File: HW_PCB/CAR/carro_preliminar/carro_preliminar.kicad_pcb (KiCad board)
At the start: 2 copper layers, 53.7 x 34.7 mm, 38 parts, among them IC1 TB6612FNG, J1 V_Battery, J2 STLINK, J3 Motores, J5 UART, J6 Servo_Motor, J7 Conn_02x04_Odd_Even, SW1 SW_DPST_x2, U1 STM32F103C8Tx, U2 AMS1117-3.3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

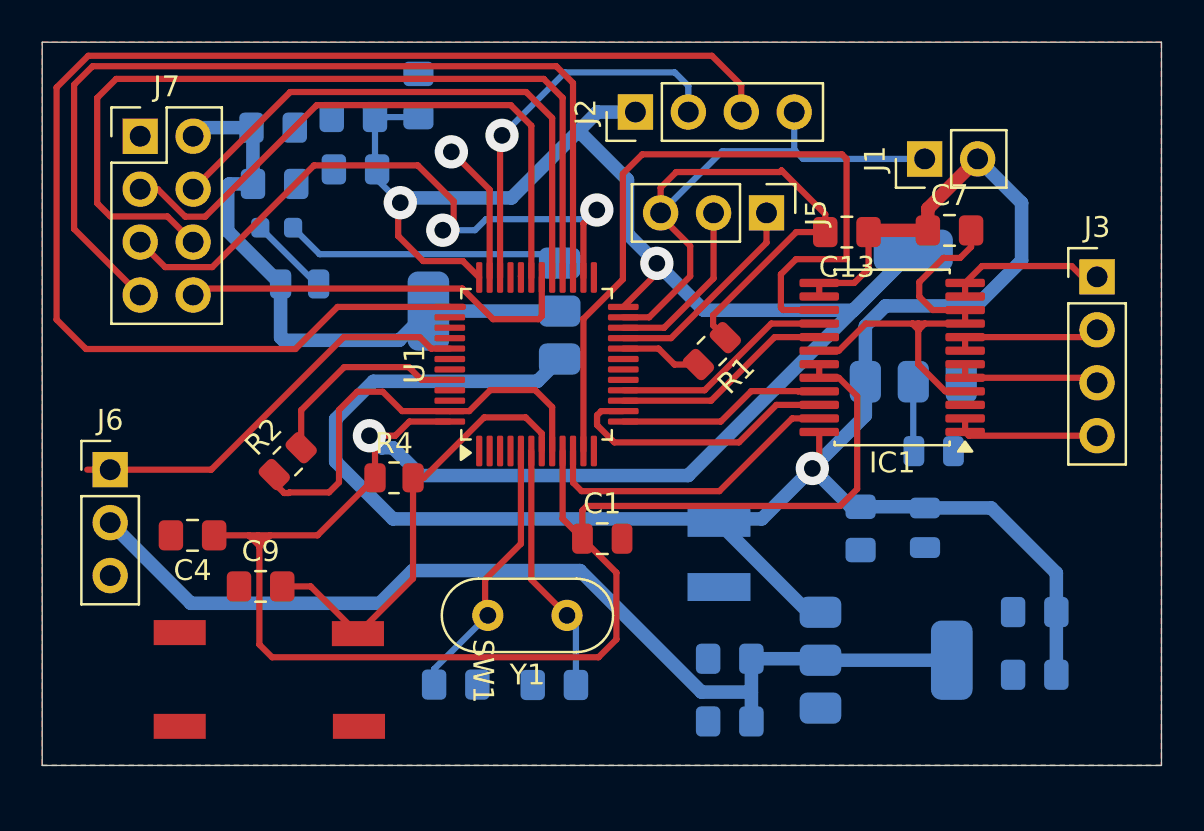
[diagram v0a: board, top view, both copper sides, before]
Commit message: Añadido divisor de tension para bateria, y conectir para luces indicadoras de bateria
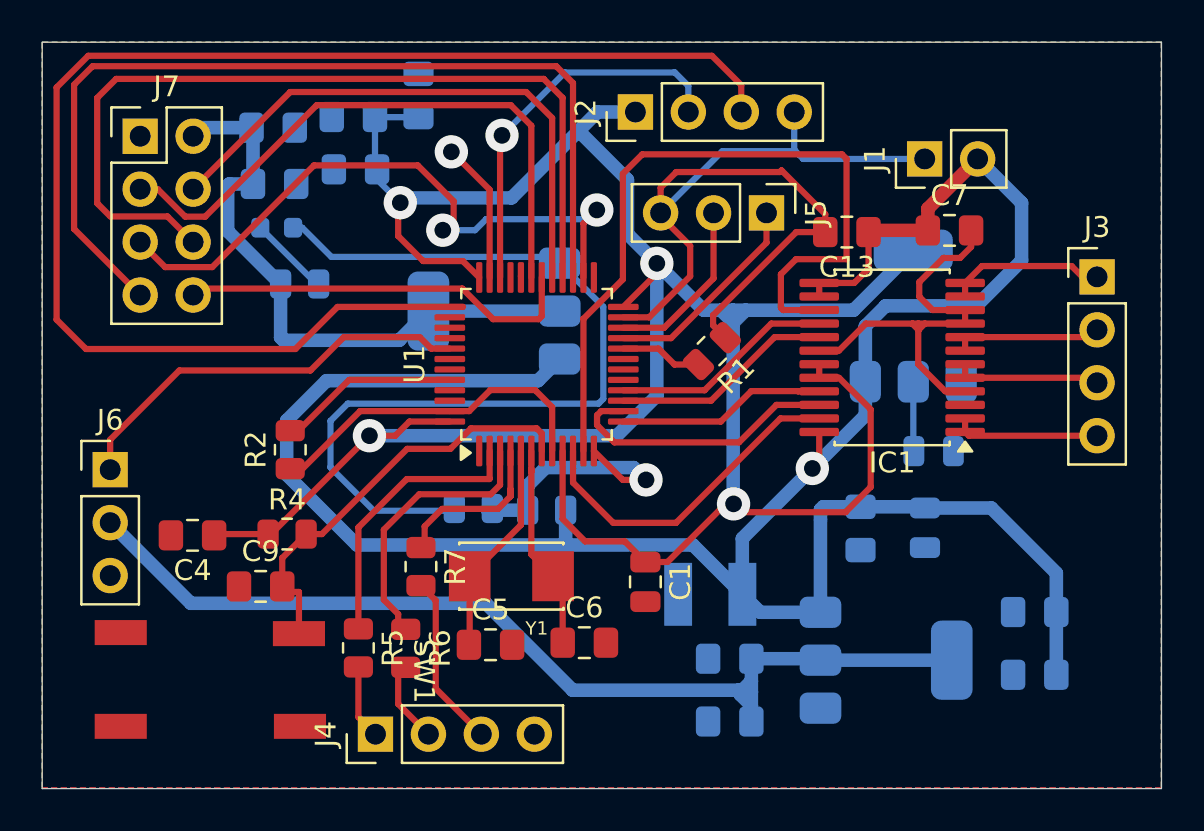
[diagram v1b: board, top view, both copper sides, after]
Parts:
- added J4: BATTLEDS, Connector_PinHeader_2.54mm:PinHeader_1x04_P2.54mm_Vertical, F.Cu at (152.5, 104.4)
- added R5: 220, Resistor_SMD:R_0805_2012Metric, F.Cu at (151.7, 100.3)
- added R6: 220, Resistor_SMD:R_0805_2012Metric, F.Cu at (154.0, 100.3)
- added R7: 220, Resistor_SMD:R_0805_2012Metric, F.Cu at (154.7, 96.4)
- added R8: PORDEFINIR, Resistor_SMD:R_0805_2012Metric, B.Cu at (160.7, 93.7)
- added R9: PORDEFINIR, Resistor_SMD:R_0805_2012Metric, B.Cu at (157.2, 93.6)
- C5, C6: moved to F.Cu
- J7: value Conn_02x04_Odd_Even -> NRF24L01
- Y1: footprint Crystal:Crystal_HC52-U_Vertical -> NX5032GA-8.000M-STD-CSU-1:XTAL_NX5032GA-8.000M-STD-CSU-1
- moved R4 5.80 mm to (148.3, 94.8)
- moved Y1 3.27 mm to (159.0, 96.8)
- moved C1 2.93 mm to (165.5, 97.1), turned to -90 degrees
- moved SW1 2.83 mm to (154.3, 101.4)
- moved C5 2.54 mm to (158.0, 100.1)
- moved C6 2.49 mm to (162.5, 100.0), turned to 0 degrees
- moved C3_Driver1 1.94 mm to (168.6, 97.7), turned to 0 degrees
- moved R2 0.56 mm to (148.4, 90.8), turned to 90 degrees
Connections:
- U1 pad 2: PC13 -> RED
- U1 pad 3: PC14 -> YELLOW
- U1 pad 4: PC15 -> GREEN
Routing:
- net VCC: track 158.6 -> 129.0 mm, vias 3 -> 4
- net GND: track 105.5 -> 131.0 mm
- net RED: track 0.00 -> 13.5 mm
- net YELLOW: track 0.00 -> 13.3 mm
- net VIN: track 101.0 -> 113.6 mm
- net PA2: track 0.00 -> 12.3 mm, vias 0 -> 1
- net Net-(J4-Pin_3): track 0.00 -> 8.33 mm
- net GREEN: track 0.00 -> 8.32 mm
- net Net-(J4-Pin_1): track 0.00 -> 3.57 mm
- net Net-(J4-Pin_2): track 0.00 -> 3.45 mm
- net OSC_IN: track 13.0 -> 10.3 mm
- net OSC_OUT: track 12.1 -> 9.98 mm
- net NRST: track 21.7 -> 20.2 mm
- net Net-(U1-BOOT0): track 10.0 -> 8.66 mm
- net PA0: track 14.9 -> 16.2 mm
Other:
- board size 53.7 x 34.7 mm -> 53.7 x 35.8 mm

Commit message: PCBCAR FULL
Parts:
- added J8: Conn_01x03_Pin, Connector_PinHeader_2.54mm:PinHeader_1x03_P2.54mm_Vertical, F.Cu at (144.3, 92.3)
- moved C4 1.41 mm to (143.6, 96.3), turned to -90 degrees
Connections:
- U1 pad 42: PB6 -> LUZ
- U1 pad 43: PB7 -> STOP
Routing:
- net STOP: track 0.00 -> 13.0 mm
- net LUZ: track 0.00 -> 12.2 mm
- net PB5: track 20.0 -> 22.9 mm
- net VCC: track 129.0 -> 130.3 mm
- net SWCLK: track 67.4 -> 66.4 mm

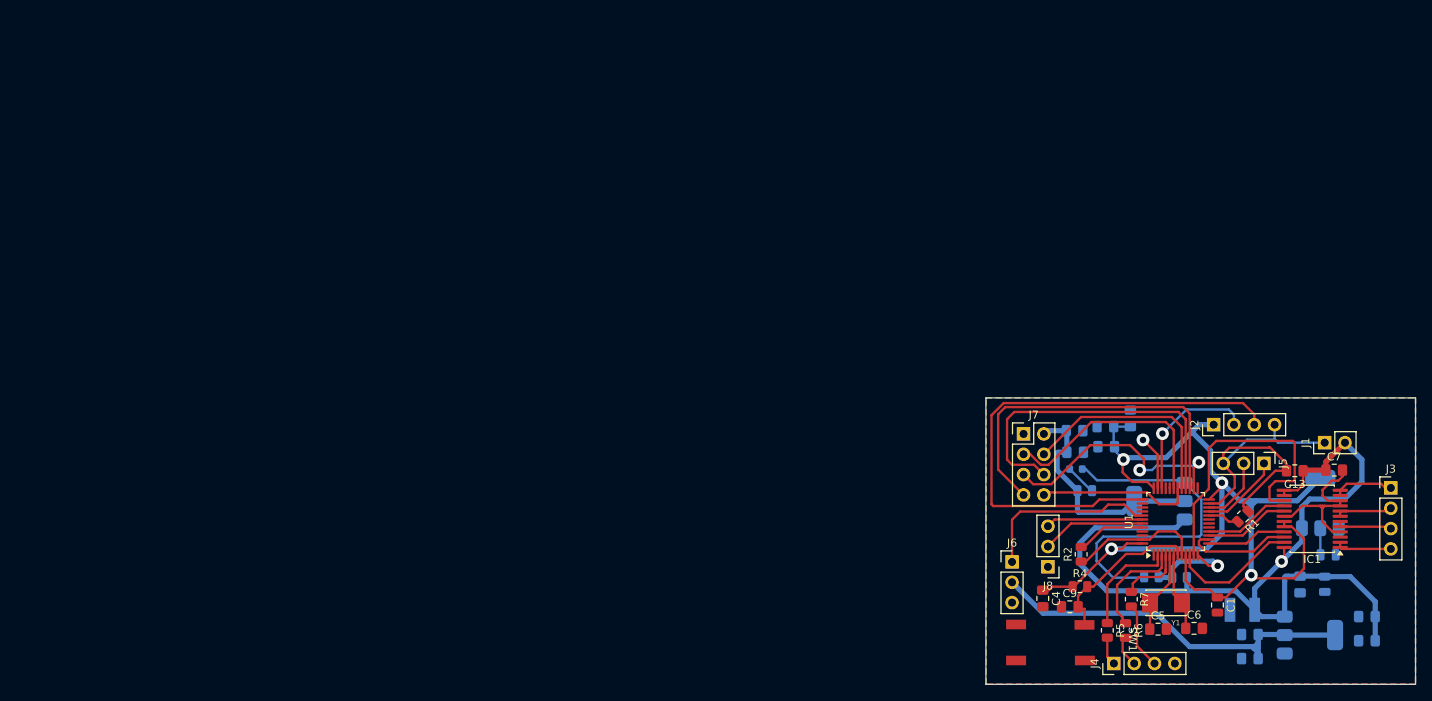
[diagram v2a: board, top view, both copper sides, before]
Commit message: Añadidos hoyos placa carro
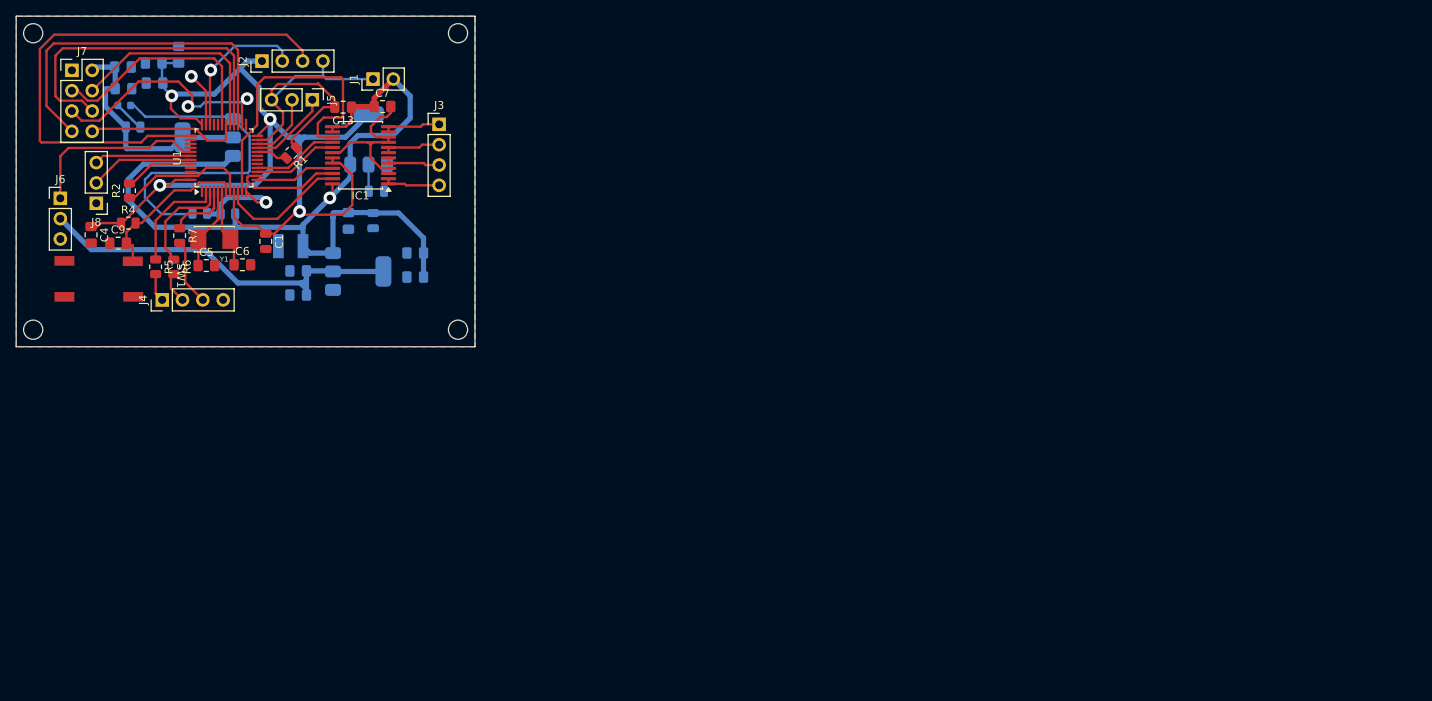
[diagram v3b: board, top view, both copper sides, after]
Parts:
- moved C1 127.3 mm to (46.5, 51.6)
- moved C12 127.3 mm to (56.8, 49.1)
- moved C13 127.3 mm to (56.2, 34.9)
- moved C1_Driver1 127.3 mm to (59.9, 49.0)
- moved C4 127.3 mm to (24.7, 50.8)
- moved C5 127.3 mm to (39.1, 54.7)
- moved C6 127.3 mm to (43.6, 54.6)
- moved C7 127.3 mm to (61.1, 34.8)
- moved C8 127.3 mm to (32.6, 31.9)
- moved C9 127.3 mm to (28.0, 51.9)
- moved D1 127.3 mm to (28.8, 34.6)
- moved IC1 127.3 mm to (58.3, 40.9)
- moved J1 127.3 mm to (59.9, 31.4)
- moved J5 127.3 mm to (52.3, 33.9)
- moved J6 127.3 mm to (20.8, 46.3)
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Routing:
- net VIN: track 113.6 -> 112.6 mm
- net SWCLK: track 66.4 -> 67.1 mm
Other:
- board size 53.7 x 35.8 mm -> 57.4 x 41.3 mm
